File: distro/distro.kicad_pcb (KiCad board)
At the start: 2 copper layers, 59.1 x 76.8 mm, 20 parts, among them K1 CONN_3, K2 CONN_3, K3 CONN_3, K4 CONN_3, P4 CONN_2, P5 CONN_2, P6 CONN_2, P7 CONN_2, P8 CONN_2

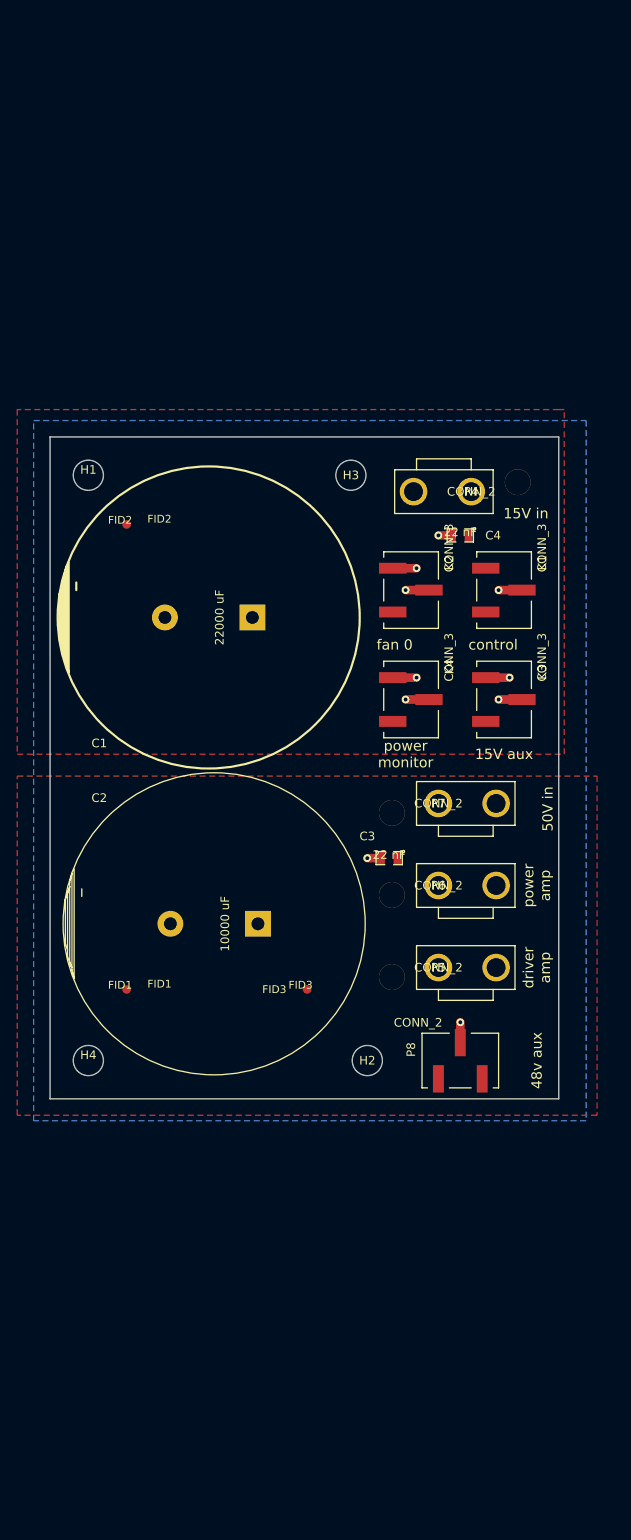
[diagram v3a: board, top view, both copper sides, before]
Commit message: added scripts for using gerbmerge for panelizing boards to reduce assembly costs
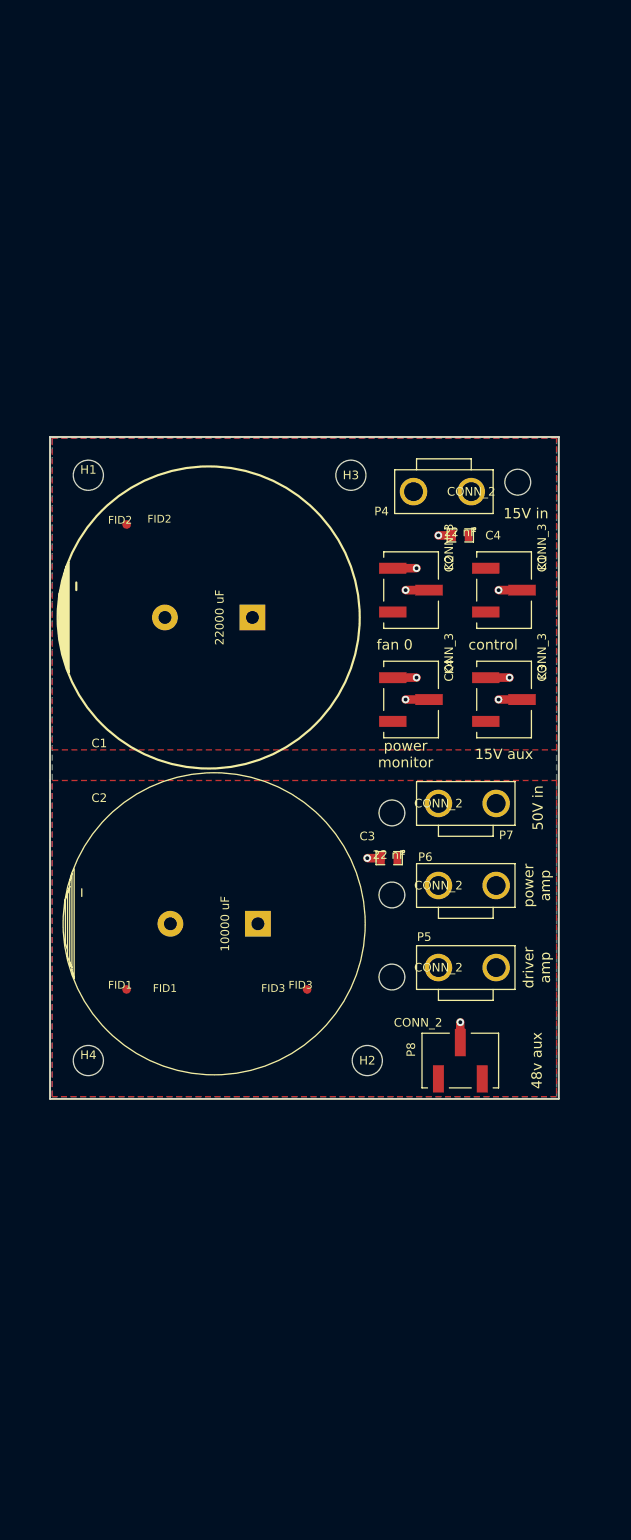
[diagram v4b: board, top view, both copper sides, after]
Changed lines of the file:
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@@
     (links 26)
     (no_connects 0)
-    (area 73.025 58.7375 140.335001 141.287501)
+    (area 74.829572 61.812499 137.247572 140.38276)
     (thickness 1.6)
-    (drawings 14)
+    (drawings 19)
     (tracks 20)
     (zones 0)
@@
     (mod_text_size 1 1)
     (mod_text_width 0.25)
-    (pad_size 3.2 3.2)
-    (pad_drill 1.9304)
+    (pad_size 3.50012 3.50012)
+    (pad_drill 3.50012)
     (pad_to_mask_clearance 0)
     (aux_axis_origin 0 0)
@@
   (module local:0015311026 (layer F.Cu)
     (at 121.92 113.9825 180)
-    (fp_text reference P6 (at 0 0 180) (layer F.SilkS)
+    (fp_text reference P6 (at 1.524 3.302 180) (layer F.SilkS)
       (effects (font (size 1 1) (thickness 0.25)))
     )
@@
     (pad 1 thru_hole circle (at -6.7 0 180) (size 3.2 3.2) (drill 2.2) (layers *.Cu *.Mask F.SilkS)
       (net 2 GND))
-    (pad 3 thru_hole circle (at 5.4 -1.1 180) (size 3 3) (drill 3) (layers *.Cu *.Mask F.SilkS))
+    (pad "" np_thru_hole circle (at 5.4 -1.1 180) (size 3 3) (drill 3) (layers *.Cu *.Mask F.SilkS))
   )
   (module local:0015311026 (layer F.Cu)
     (at 121.92 104.4575 180)
-    (fp_text reference P7 (at 0 0 180) (layer F.SilkS)
+    (fp_text reference P7 (at -7.874 -3.683 360) (layer F.SilkS)
       (effects (font (size 1 1) (thickness 0.25)))
     )
@@
     (pad 1 thru_hole circle (at -6.7 0 180) (size 3.2 3.2) (drill 2.2) (layers *.Cu *.Mask F.SilkS)
       (net 2 GND))
-    (pad 3 thru_hole circle (at 5.4 -1.1 180) (size 3 3) (drill 3) (layers *.Cu *.Mask F.SilkS))
+    (pad "" np_thru_hole circle (at 5.4 -1.1 180) (size 3 3) (drill 3) (layers *.Cu *.Mask F.SilkS))
   )
   (module sdtransmitter:0740991003 (layer F.Cu)
@@
     )
     (fp_circle (center 0 0) (end 3.50012 0) (layer Cmts.User) (width 0.381))
-    (pad 1 thru_hole circle (at 0 0) (size 3.50012 3.50012) (drill 3.50012) (layers))
+    (pad "" np_thru_hole circle (at 0 0) (size 3.50012 3.50012) (drill 3.50012) (layers *.Cu *.Mask F.SilkS))
   )
   (module Mounting_Holes:MountingHole_3-5mm (layer F.Cu)
@@
     )
     (fp_circle (center 0 0) (end 3.50012 0) (layer Cmts.User) (width 0.381))
-    (pad 1 thru_hole circle (at 0 0) (size 3.50012 3.50012) (drill 3.50012) (layers))
+    (pad "" np_thru_hole circle (at 0 0) (size 3.50012 3.50012) (drill 3.50012) (layers *.Cu *.Mask F.SilkS))
   )
   (module Mounting_Holes:MountingHole_3-5mm (layer F.Cu)
@@
     )
     (fp_circle (center 0 0) (end 3.50012 0) (layer Cmts.User) (width 0.381))
-    (pad 1 thru_hole circle (at 0 0) (size 3.50012 3.50012) (drill 3.50012) (layers))
+    (pad "" np_thru_hole circle (at 0 0) (size 3.50012 3.50012) (drill 3.50012) (layers *.Cu *.Mask F.SilkS))
   )
   (module Mounting_Holes:MountingHole_3-5mm (layer F.Cu)
@@
     )
     (fp_circle (center 0 0) (end 3.50012 0) (layer Cmts.User) (width 0.381))
-    (pad 1 thru_hole circle (at 0 0) (size 3.50012 3.50012) (drill 3.50012) (layers))
+    (pad "" np_thru_hole circle (at 0 0) (size 3.50012 3.50012) (drill 3.50012) (layers *.Cu *.Mask F.SilkS))
   )
   (module SMD_Packages:SMD-0805 (layer F.Cu)
@@
   (module local:0015311026 (layer F.Cu)
     (at 125.73 68.2625)
-    (fp_text reference P4 (at 0 0) (layer F.SilkS)
+    (fp_text reference P4 (at -10.414 2.286) (layer F.SilkS)
       (effects (font (size 1 1) (thickness 0.25)))
     )
@@
     (pad 1 thru_hole circle (at -6.7 0) (size 3.2 3.2) (drill 2.2) (layers *.Cu *.Mask F.SilkS)
       (net 2 GND))
-    (pad 3 thru_hole circle (at 5.4 -1.1) (size 3 3) (drill 3) (layers *.Cu *.Mask F.SilkS))
+    (pad "" np_thru_hole circle (at 5.4 -1.1) (size 3 3) (drill 3) (layers *.Cu *.Mask F.SilkS))
   )
   (module local:0015311026 (layer F.Cu)
     (at 121.92 123.5075 180)
-    (fp_text reference P5 (at 0 0 180) (layer F.SilkS)
+    (fp_text reference P5 (at 1.651 3.556 180) (layer F.SilkS)
       (effects (font (size 1 1) (thickness 0.25)))
     )
@@
     (pad 1 thru_hole circle (at -6.7 0 180) (size 3.2 3.2) (drill 2.2) (layers *.Cu *.Mask F.SilkS)
       (net 2 GND))
-    (pad 3 thru_hole circle (at 5.4 -1.1 180) (size 3 3) (drill 3) (layers *.Cu *.Mask F.SilkS))
+    (pad "" np_thru_hole circle (at 5.4 -1.1 180) (size 3 3) (drill 3) (layers *.Cu *.Mask F.SilkS))
   )
   (module sdtransmitter:0740991003 (layer F.Cu)
@@
   (module sdtransmitter:FID_1MM (layer F.Cu)
     (at 85.725 126.0475)
-    (fp_text reference FID1 (at 3.81 -0.635) (layer F.SilkS)
+    (fp_text reference FID1 (at 4.445 -0.127) (layer F.SilkS)
       (effects (font (size 0.9 0.9) (thickness 0.225)))
     )
@@
   (module sdtransmitter:FID_1MM (layer F.Cu)
     (at 106.68 126.0475)
-    (fp_text reference FID3 (at -3.81 0) (layer F.SilkS)
+    (fp_text reference FID3 (at -3.937 -0.127) (layer F.SilkS)
       (effects (font (size 0.9 0.9) (thickness 0.225)))
     )
@@
       (solder_mask_margin 1.5))
   )
+  (gr_line (start 76.835 138.7475) (end 76.835 101.7905) (angle 90) (layer F.SilkS) (width 0.2))
+  (gr_line (start 135.89 138.7475) (end 76.835 138.7475) (angle 90) (layer F.SilkS) (width 0.2))
+  (gr_line (start 135.89 61.9125) (end 135.89 138.7475) (angle 90) (layer F.SilkS) (width 0.2))
+  (gr_line (start 76.835 61.9125) (end 135.89 61.9125) (angle 90) (layer F.SilkS) (width 0.2))
+  (gr_line (start 76.835 101.7905) (end 76.835 61.9125) (angle 90) (layer F.SilkS) (width 0.2))
   (gr_line (start 135.89 138.7475) (end 135.89 61.9125) (angle 90) (layer Edge.Cuts) (width 0.1))
   (gr_line (start 76.835 138.7475) (end 135.89 138.7475) (angle 90) (layer Edge.Cuts) (width 0.1))
@@
     (effects (font (size 1.5 1.5) (thickness 0.3)) (justify mirror))
   )
-  (gr_text "50V in" (at 134.62 105.0925 90) (layer F.SilkS)
+  (gr_text "50V in" (at 133.477 104.9655 90) (layer F.SilkS)
     (effects (font (size 1.2 1.2) (thickness 0.3)))
   )
@@
     (effects (font (size 1.2 1.2) (thickness 0.3)))
   )
+  (segment (start 131.623 92.3925) (end 128.905 92.3925) (width 1) (layer F.Cu) (net 2))
+  (via (at 128.905 92.3925) (size 0.889) (layers F.Cu B.Cu) (net 2))
+  (segment (start 127.413 89.8525) (end 130.175 89.8525) (width 1) (layer F.Cu) (net 2))
+  (via (at 130.175 89.8525) (size 0.889) (layers F.Cu B.Cu) (net 2))
+  (segment (start 120.828 92.3925) (end 118.11 92.3925) (width 1) (layer F.Cu) (net 2))
+  (via (at 118.11 92.3925) (size 0.889) (layers F.Cu B.Cu) (net 2))
+  (segment (start 116.618 89.8525) (end 119.38 89.8525) (width 1) (layer F.Cu) (net 2))
+  (via (at 119.38 89.8525) (size 0.889) (layers F.Cu B.Cu) (net 2))
+  (segment (start 131.623 79.6925) (end 128.905 79.6925) (width 1) (layer F.Cu) (net 2))
+  (via (at 128.905 79.6925) (size 0.889) (layers F.Cu B.Cu) (net 2))
+  (segment (start 120.828 79.6925) (end 118.11 79.6925) (width 1) (layer F.Cu) (net 2))
+  (via (at 118.11 79.6925) (size 0.889) (layers F.Cu B.Cu) (net 2))
+  (segment (start 116.618 77.1525) (end 119.38 77.1525) (width 1) (layer F.Cu) (net 2))
+  (via (at 119.38 77.1525) (size 0.889) (layers F.Cu B.Cu) (net 2))
+  (segment (start 123.5075 73.3425) (end 121.92 73.3425) (width 1) (layer F.Cu) (net 2))
+  (via (at 121.92 73.3425) (size 0.889) (layers F.Cu B.Cu) (net 2))
+  (segment (start 124.46 132.2195) (end 124.46 129.8575) (width 1) (layer F.Cu) (net 2))
+  (via (at 124.46 129.8575) (size 0.889) (layers F.Cu B.Cu) (net 2))
+  (segment (start 115.2525 110.8075) (end 113.665 110.8075) (width 1) (layer F.Cu) (net 2))
   (via (at 113.665 110.8075) (size 0.889) (layers F.Cu B.Cu) (net 2))
-  (segment (start 115.2525 110.8075) (end 113.665 110.8075) (width 1) (layer F.Cu) (net 2))
-  (via (at 124.46 129.8575) (size 0.889) (layers F.Cu B.Cu) (net 2))
-  (segment (start 124.46 132.2195) (end 124.46 129.8575) (width 1) (layer F.Cu) (net 2))
-  (via (at 121.92 73.3425) (size 0.889) (layers F.Cu B.Cu) (net 2))
-  (segment (start 123.5075 73.3425) (end 121.92 73.3425) (width 1) (layer F.Cu) (net 2))
-  (via (at 119.38 77.1525) (size 0.889) (layers F.Cu B.Cu) (net 2))
-  (segment (start 116.618 77.1525) (end 119.38 77.1525) (width 1) (layer F.Cu) (net 2))
-  (via (at 118.11 79.6925) (size 0.889) (layers F.Cu B.Cu) (net 2))
-  (segment (start 120.828 79.6925) (end 118.11 79.6925) (width 1) (layer F.Cu) (net 2))
-  (via (at 128.905 79.6925) (size 0.889) (layers F.Cu B.Cu) (net 2))
-  (segment (start 131.623 79.6925) (end 128.905 79.6925) (width 1) (layer F.Cu) (net 2))
-  (via (at 119.38 89.8525) (size 0.889) (layers F.Cu B.Cu) (net 2))
-  (segment (start 116.618 89.8525) (end 119.38 89.8525) (width 1) (layer F.Cu) (net 2))
-  (via (at 118.11 92.3925) (size 0.889) (layers F.Cu B.Cu) (net 2))
-  (segment (start 120.828 92.3925) (end 118.11 92.3925) (width 1) (layer F.Cu) (net 2))
-  (via (at 130.175 89.8525) (size 0.889) (layers F.Cu B.Cu) (net 2))
-  (segment (start 127.413 89.8525) (end 130.175 89.8525) (width 1) (layer F.Cu) (net 2))
-  (via (at 128.905 92.3925) (size 0.889) (layers F.Cu B.Cu) (net 2))
-  (segment (start 131.623 92.3925) (end 128.905 92.3925) (width 1) (layer F.Cu) (net 2))
   (zone (net 2) (net_name GND) (layer B.Cu) (hatch edge 0.508)
     (connect_pads (clearance 0.5))
@@
     (polygon
       (pts
-        (xy 139.065 141.2875) (xy 74.93 141.2875) (xy 74.93 60.0075) (xy 139.065 60.0075)
+        (xy 135.636 138.4935) (xy 77.089 138.4935) (xy 77.089 62.0395) (xy 135.636 62.0395)
       )
     )
@@
     (polygon
       (pts
-        (xy 73.025 58.7375) (xy 73.025 98.7425) (xy 136.525 98.7425) (xy 136.525 58.7375) (xy 135.89 58.7375)
+        (xy 77.089 98.2345) (xy 135.636 98.2345) (xy 135.636 62.0395) (xy 77.089 62.0395) (xy 77.089 62.1665)
       )
     )
@@
     (polygon
       (pts
-        (xy 140.335 140.6525) (xy 73.025 140.6525) (xy 73.025 101.2825) (xy 140.335 101.2825)
+        (xy 77.089 101.7905) (xy 135.636 101.7905) (xy 135.636 138.4935) (xy 77.089 138.4935)
       )
     )

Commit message: DFM changes after last protoype rev
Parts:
- removed P8: CONN_2, sdtransmitter:0740991003
- moved P5 10.7 mm to (125.7, 133.5)
- moved P6 6.55 mm to (125.7, 119.3)
- moved P7 3.86 mm to (125.7, 105.1)
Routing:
- net GND: track 24.7 -> 22.3 mm, vias 10 -> 9
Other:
- board text removed: "48v aux"
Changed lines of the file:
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@@
 (kicad_pcb (version 3) (host pcbnew "(2014-03-19 BZR 4756)-product")
   (general
-    (links 26)
+    (links 24)
     (no_connects 0)
-    (area 74.829572 61.812499 137.247572 140.38276)
+    (area 76.784999 61.862499 135.940001 138.797501)
     (thickness 1.6)
-    (drawings 19)
-    (tracks 20)
+    (drawings 18)
+    (tracks 18)
     (zones 0)
-    (modules 20)
+    (modules 19)
     (nets 4)
   )
@@
   )
   (module local:0015311026 (layer F.Cu)
-    (at 121.92 113.9825 180)
-    (fp_text reference P6 (at 1.524 3.302 180) (layer F.SilkS)
+    (at 125.73 119.3165 180)
+    (fp_text reference P6 (at 4.572 -4.064 180) (layer F.SilkS)
       (effects (font (size 1 1) (thickness 0.25)))
     )
@@
   )
   (module local:0015311026 (layer F.Cu)
-    (at 121.92 104.4575 180)
-    (fp_text reference P7 (at -7.874 -3.683 360) (layer F.SilkS)
+    (at 125.73 105.0925 180)
+    (fp_text reference P7 (at 4.064 -3.556 360) (layer F.SilkS)
       (effects (font (size 1 1) (thickness 0.25)))
     )
@@
     (pad "" np_thru_hole circle (at 5.4 -1.1 180) (size 3 3) (drill 3) (layers *.Cu *.Mask F.SilkS))
   )
-  (module sdtransmitter:0740991003 (layer F.Cu)
-    (at 124.46 134.3025)
-    (fp_text reference P8 (at -5.715 -1.27 90) (layer F.SilkS)
-      (effects (font (size 1 1) (thickness 0.25)))
-    )
-    (fp_text value CONN_2 (at -4.9 -4.4) (layer F.SilkS)
-      (effects (font (size 1 1) (thickness 0.25)))
-    )
-    (fp_line (start -1.27 3.175) (end 1.27 3.175) (layer F.SilkS) (width 0.15))
-    (fp_line (start -4.445 -3.175) (end -1.27 -3.175) (layer F.SilkS) (width 0.15))
-    (fp_line (start -3.81 3.175) (end -4.445 3.175) (layer F.SilkS) (width 0.15))
-    (fp_line (start -4.445 3.175) (end -4.445 -3.175) (layer F.SilkS) (width 0.15))
-    (fp_line (start 1.27 -3.175) (end 4.445 -3.175) (layer F.SilkS) (width 0.15))
-    (fp_line (start 4.445 -3.175) (end 4.445 3.175) (layer F.SilkS) (width 0.15))
-    (fp_line (start 4.445 3.175) (end 3.81 3.175) (layer F.SilkS) (width 0.15))
-    (pad 1 smd rect (at -2.54 2.127) (size 1.27 3.18) (layers F.Cu F.Paste F.Mask)
-      (net 3 VCC))
-    (pad 2 smd rect (at 0 -2.083) (size 1.27 3.18) (layers F.Cu F.Paste F.Mask)
-      (net 2 GND))
-    (pad 3 smd rect (at 2.54 2.127) (size 1.27 3.18) (layers F.Cu F.Paste F.Mask))
-  )
   (module Mounting_Holes:MountingHole_3-5mm (layer F.Cu)
     (at 81.28 66.3575)
@@
   )
   (module local:0015311026 (layer F.Cu)
-    (at 121.92 123.5075 180)
-    (fp_text reference P5 (at 1.651 3.556 180) (layer F.SilkS)
+    (at 125.73 133.5405 180)
+    (fp_text reference P5 (at 6.604 -3.556 180) (layer F.SilkS)
       (effects (font (size 1 1) (thickness 0.25)))
     )
@@
     (effects (font (size 1.5 1.5) (thickness 0.3)) (justify mirror))
   )
-  (gr_text "50V in" (at 133.477 104.9655 90) (layer F.SilkS)
-    (effects (font (size 1.2 1.2) (thickness 0.3)))
-  )
-  (gr_text "driver\namp" (at 133.35 123.5075 90) (layer F.SilkS)
-    (effects (font (size 1.2 1.2) (thickness 0.3)))
-  )
-  (gr_text "power\namp" (at 133.35 113.9825 90) (layer F.SilkS)
-    (effects (font (size 1.2 1.2) (thickness 0.3)))
+  (gr_text "50V in" (at 117.602 104.5845 90) (layer F.SilkS)
+    (effects (font (size 1 1) (thickness 0.25)))
+  )
+  (gr_text "driver amp" (at 117.602 120.8405 90) (layer F.SilkS)
+    (effects (font (size 1 1) (thickness 0.25)))
+  )
+  (gr_text "power\namp" (at 118.11 130.4925 90) (layer F.SilkS)
+    (effects (font (size 1 1) (thickness 0.25)))
   )
   (gr_text "15V in" (at 132.08 70.8025) (layer F.SilkS)
@@
     (effects (font (size 1.2 1.2) (thickness 0.3)))
   )
-  (gr_text "48v aux" (at 133.35 134.3025 90) (layer F.SilkS)
-    (effects (font (size 1.2 1.2) (thickness 0.3)))
-  )
+  (via (at 113.665 110.8075) (size 0.889) (layers F.Cu B.Cu) (net 2))
+  (segment (start 115.2525 110.8075) (end 113.665 110.8075) (width 1) (layer F.Cu) (net 2))
+  (via (at 121.92 73.3425) (size 0.889) (layers F.Cu B.Cu) (net 2))
+  (segment (start 123.5075 73.3425) (end 121.92 73.3425) (width 1) (layer F.Cu) (net 2))
+  (via (at 119.38 77.1525) (size 0.889) (layers F.Cu B.Cu) (net 2))
+  (segment (start 116.618 77.1525) (end 119.38 77.1525) (width 1) (layer F.Cu) (net 2))
+  (via (at 118.11 79.6925) (size 0.889) (layers F.Cu B.Cu) (net 2))
+  (segment (start 120.828 79.6925) (end 118.11 79.6925) (width 1) (layer F.Cu) (net 2))
+  (via (at 128.905 79.6925) (size 0.889) (layers F.Cu B.Cu) (net 2))
+  (segment (start 131.623 79.6925) (end 128.905 79.6925) (width 1) (layer F.Cu) (net 2))
+  (via (at 119.38 89.8525) (size 0.889) (layers F.Cu B.Cu) (net 2))
+  (segment (start 116.618 89.8525) (end 119.38 89.8525) (width 1) (layer F.Cu) (net 2))
+  (via (at 118.11 92.3925) (size 0.889) (layers F.Cu B.Cu) (net 2))
+  (segment (start 120.828 92.3925) (end 118.11 92.3925) (width 1) (layer F.Cu) (net 2))
+  (via (at 130.175 89.8525) (size 0.889) (layers F.Cu B.Cu) (net 2))
+  (segment (start 127.413 89.8525) (end 130.175 89.8525) (width 1) (layer F.Cu) (net 2))
+  (via (at 128.905 92.3925) (size 0.889) (layers F.Cu B.Cu) (net 2))
   (segment (start 131.623 92.3925) (end 128.905 92.3925) (width 1) (layer F.Cu) (net 2))
-  (via (at 128.905 92.3925) (size 0.889) (layers F.Cu B.Cu) (net 2))
-  (segment (start 127.413 89.8525) (end 130.175 89.8525) (width 1) (layer F.Cu) (net 2))
-  (via (at 130.175 89.8525) (size 0.889) (layers F.Cu B.Cu) (net 2))
-  (segment (start 120.828 92.3925) (end 118.11 92.3925) (width 1) (layer F.Cu) (net 2))
-  (via (at 118.11 92.3925) (size 0.889) (layers F.Cu B.Cu) (net 2))
-  (segment (start 116.618 89.8525) (end 119.38 89.8525) (width 1) (layer F.Cu) (net 2))
-  (via (at 119.38 89.8525) (size 0.889) (layers F.Cu B.Cu) (net 2))
-  (segment (start 131.623 79.6925) (end 128.905 79.6925) (width 1) (layer F.Cu) (net 2))
-  (via (at 128.905 79.6925) (size 0.889) (layers F.Cu B.Cu) (net 2))
-  (segment (start 120.828 79.6925) (end 118.11 79.6925) (width 1) (layer F.Cu) (net 2))
-  (via (at 118.11 79.6925) (size 0.889) (layers F.Cu B.Cu) (net 2))
-  (segment (start 116.618 77.1525) (end 119.38 77.1525) (width 1) (layer F.Cu) (net 2))
-  (via (at 119.38 77.1525) (size 0.889) (layers F.Cu B.Cu) (net 2))
-  (segment (start 123.5075 73.3425) (end 121.92 73.3425) (width 1) (layer F.Cu) (net 2))
-  (via (at 121.92 73.3425) (size 0.889) (layers F.Cu B.Cu) (net 2))
-  (segment (start 124.46 132.2195) (end 124.46 129.8575) (width 1) (layer F.Cu) (net 2))
-  (via (at 124.46 129.8575) (size 0.889) (layers F.Cu B.Cu) (net 2))
-  (segment (start 115.2525 110.8075) (end 113.665 110.8075) (width 1) (layer F.Cu) (net 2))
-  (via (at 113.665 110.8075) (size 0.889) (layers F.Cu B.Cu) (net 2))
   (zone (net 2) (net_name GND) (layer B.Cu) (hatch edge 0.508)
     (connect_pads (clearance 0.5))
